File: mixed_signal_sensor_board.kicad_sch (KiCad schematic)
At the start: 51 parts, among them J1 Conn_01x02, J3 Conn_01x04, J4 Conn_01x06, SW1 SW_Push, SW2 SW_Push, U1 LM27762, U2 MagI3C_171013201, U3 TMP117xxDRV, U4 TPS7A20xxxDBV, U5 TPS7A20xxxDBV, U6 ADS131M08xPBS, U7 STM32L552CEUx, Y1 SG-8018CE_8.192M-TJHSA

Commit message: 24V Regulator, Pyro Igniter Circuit
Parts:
- U3: renamed from U2; footprint (none) -> MagI3C_171013201:MagI3C_171013201
- renumbered J3 to J2, J4 to J3, R13 to R12, R12 to R13, R4 to R2, R5 to R3, R2 to R4, R3 to R5, U3 to U1, U1 to U2
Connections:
- no-connect marks 3 -> 20

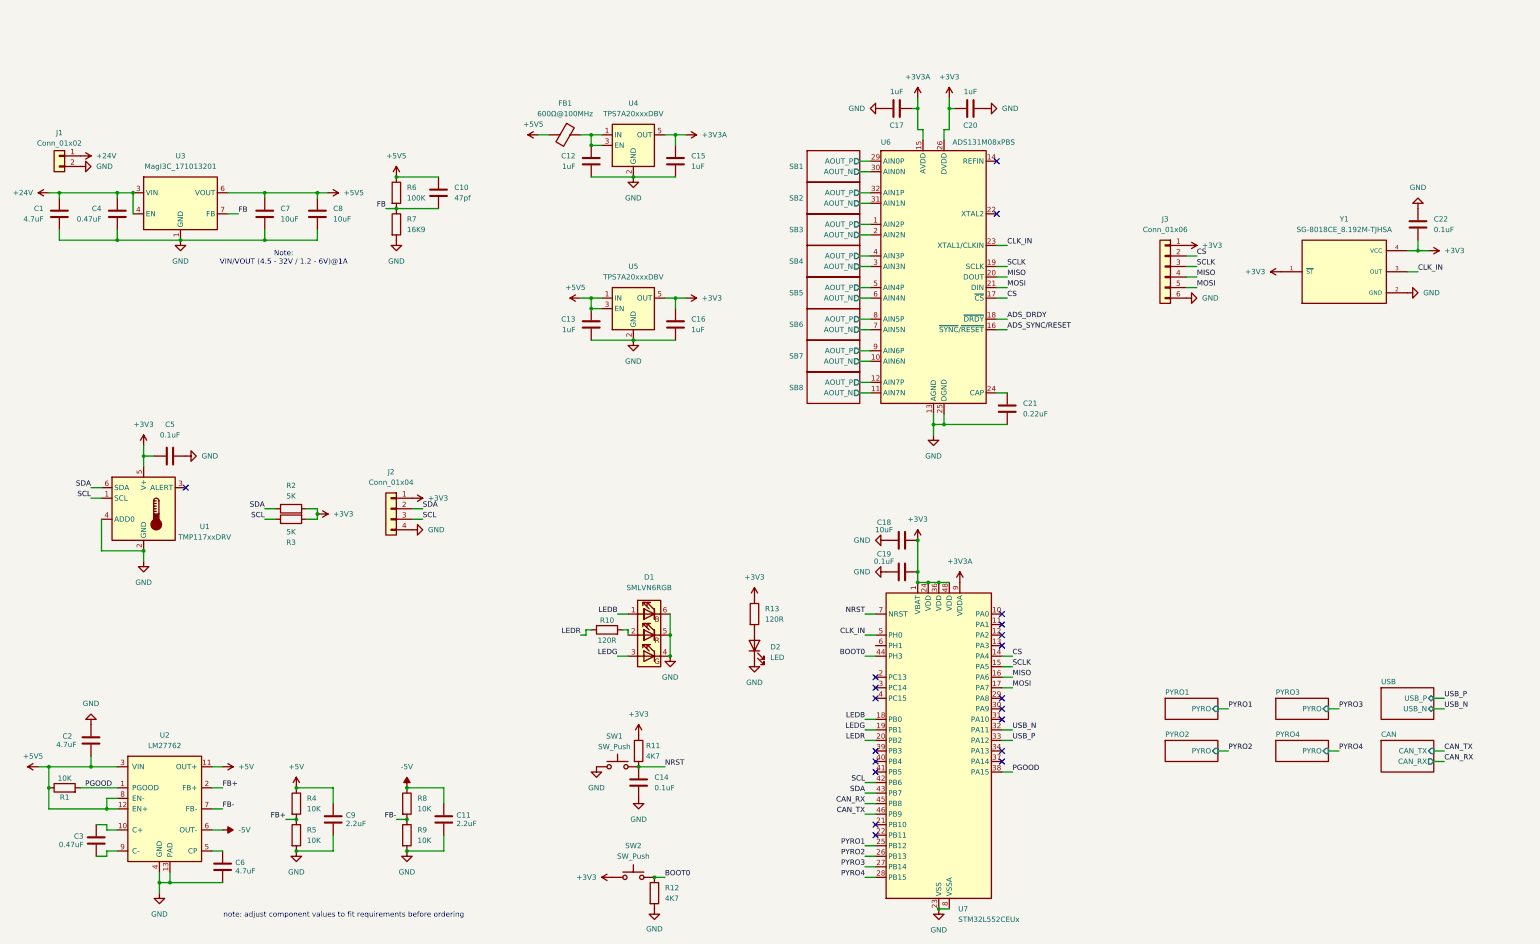
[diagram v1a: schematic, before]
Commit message: Pyro fault detection, Decoupling Caps STM32, Initial PCB Layout
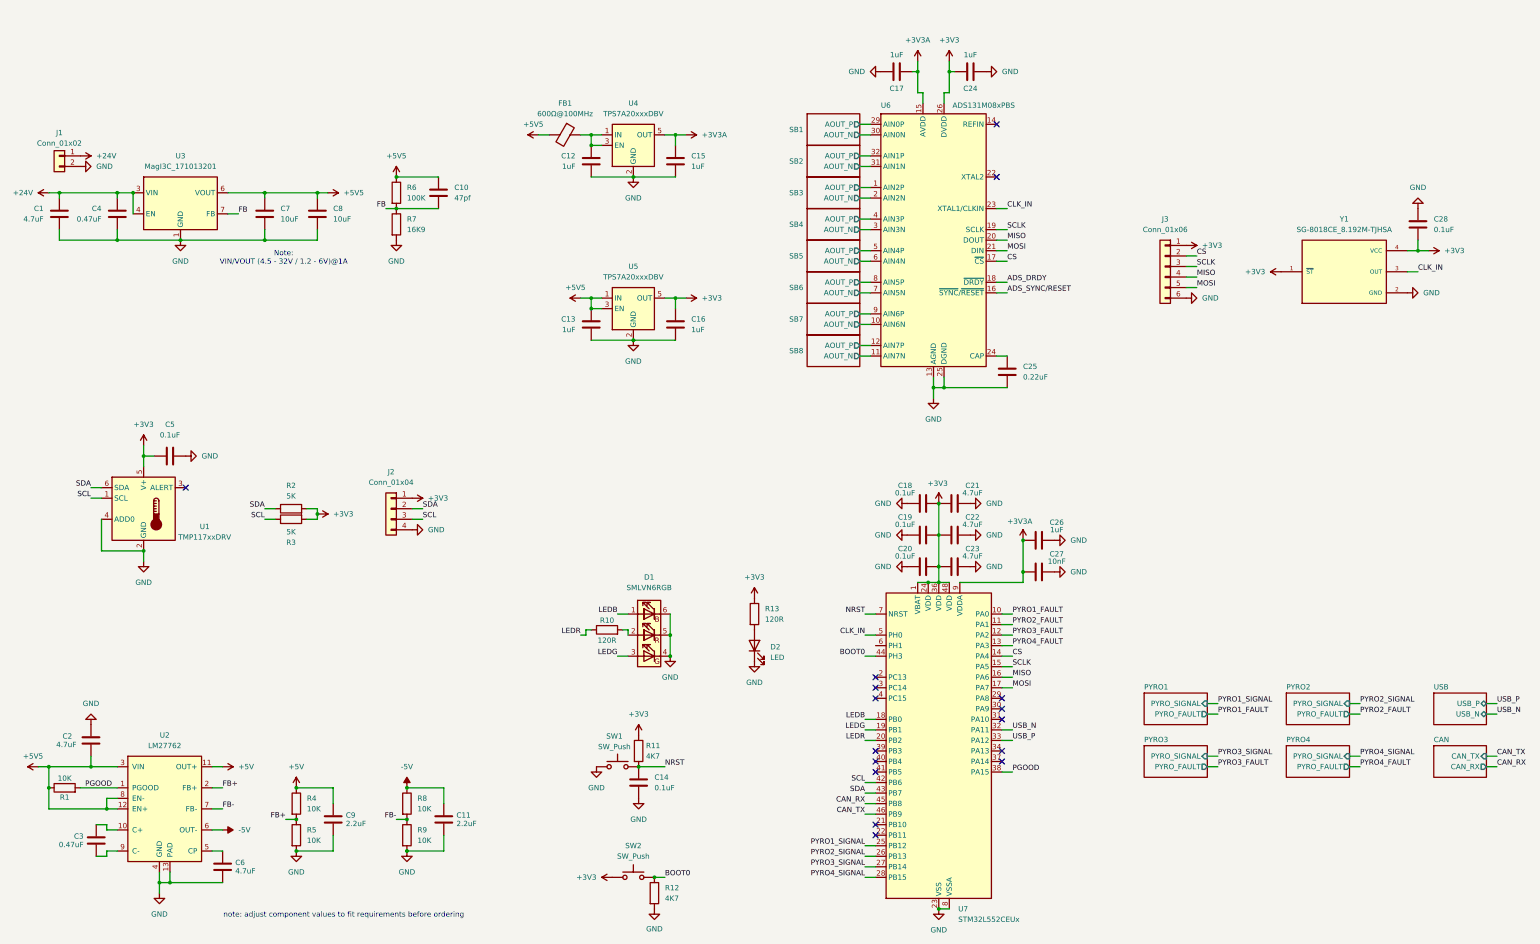
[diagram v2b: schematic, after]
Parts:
- added C20: 0.1uF, Capacitor_SMD:C_0402_1005Metric, symbol Device:C
- added C21, C22, C23: 4.7uF, Capacitor_SMD:C_0402_1005Metric, symbol Device:C
- added C26: 1uF, Capacitor_SMD:C_0402_1005Metric, symbol Device:C
- added C27: 10nF, Capacitor_SMD:C_0402_1005Metric, symbol Device:C
- C18: value 10uF -> 0.1uF
- J1: footprint Connector_JST:JST_XH_B2B-XH-A_1x02_P2.50mm_Vertical -> Connector_JST:JST_XH_S2B-XH-A_1x02_P2.50mm_Horizontal
- J2: footprint Connector_JST:JST_XH_B4B-XH-A_1x04_P2.50mm_Vertical -> Connector_JST:JST_XH_S4B-XH-A_1x04_P2.50mm_Horizontal
- J3: footprint Connector_JST:JST_XH_B6B-XH-A_1x06_P2.50mm_Vertical -> Connector_JST:JST_XH_S6B-XH-A_1x06_P2.50mm_Horizontal
- renumbered C20 to C24, C21 to C25, C22 to C28
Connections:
- net +3V3: now also C20.2, C21.2, C22.2, C23.2
- net +3V3A: now also C26.2, C27.2
- net GND: now also C20.1, C21.1, C22.1, C23.1, C26.1, C27.1
- net PYRO1_FAULT: now reaches U7.10 (PA0)
- net PYRO2_FAULT: now reaches U7.11 (PA1)
- net PYRO3_FAULT: now reaches U7.12 (PA2)
- net PYRO4_FAULT: now reaches U7.13 (PA3)
- net PYRO1 renamed PYRO1_SIGNAL
- net PYRO2 renamed PYRO2_SIGNAL
- net PYRO3 renamed PYRO3_SIGNAL
- net PYRO4 renamed PYRO4_SIGNAL
- no-connect marks 20 -> 16
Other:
- sheet PYRO1 ports: added PYRO_FAULT, PYRO_SIGNAL; removed PYRO
- sheet PYRO2 ports: added PYRO_FAULT, PYRO_SIGNAL; removed PYRO
- sheet PYRO3 ports: added PYRO_FAULT, PYRO_SIGNAL; removed PYRO
- sheet PYRO4 ports: added PYRO_FAULT, PYRO_SIGNAL; removed PYRO
- moved on the sheet: C17, C24, C25, U6

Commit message: Finished first rough initial layout
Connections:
- net ADS_DRDY: now also U7.10 (PA0)
- net ADS_SYNC/RESET: now also U7.11 (PA1)
- net LEDB: now also U7.41 (PB5); no longer U7.18 (PB0)
- net LEDG: now also U7.39 (PB3); no longer U7.19 (PB1)
- net LEDR: now also U7.40 (PB4); no longer U7.20 (PB2)
- net PYRO1_FAULT: now also U7.19 (PB1); no longer U7.10 (PA0)
- net PYRO1_SIGNAL: now also U7.18 (PB0); no longer U7.25 (PB12)
- net PYRO2_FAULT: now also U7.21 (PB10); no longer U7.11 (PA1)
- net PYRO2_SIGNAL: now also U7.20 (PB2); no longer U7.26 (PB13)
- net PYRO3_FAULT: now also U7.28 (PB15); no longer U7.12 (PA2)
- net PYRO3_SIGNAL: now also U7.29 (PA8); no longer U7.27 (PB14)
- net PYRO4_FAULT: now also U7.30 (PA9); no longer U7.13 (PA3)
- net PYRO4_SIGNAL: now also U7.31 (PA10); no longer U7.28 (PB15)
- no-connect marks 16 -> 14

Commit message: Step files, SMD connectors, reduced size
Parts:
- J1: footprint Connector_JST:JST_XH_S2B-XH-A_1x02_P2.50mm_Horizontal -> Connector_JST:JST_PH_S2B-PH-SM4-TB_1x02-1MP_P2.00mm_Horizontal
- J2: footprint Connector_JST:JST_XH_S4B-XH-A_1x04_P2.50mm_Horizontal -> Connector_JST:JST_PH_S4B-PH-SM4-TB_1x04-1MP_P2.00mm_Horizontal
- J3: footprint Connector_JST:JST_XH_S6B-XH-A_1x06_P2.50mm_Horizontal -> Connector_JST:JST_PH_S6B-PH-SM4-TB_1x06-1MP_P2.00mm_Horizontal
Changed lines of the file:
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@@
 			)
 		)
-		(property "Footprint" "Connector_JST:JST_XH_S6B-XH-A_1x06_P2.50mm_Horizontal"
+		(property "Footprint" "Connector_JST:JST_PH_S6B-PH-SM4-TB_1x06-1MP_P2.00mm_Horizontal"
 			(at 309.88 93.98 0)
 			(hide yes)
@@
 			)
 		)
-		(property "Footprint" "Connector_JST:JST_XH_S4B-XH-A_1x04_P2.50mm_Horizontal"
+		(property "Footprint" "Connector_JST:JST_PH_S4B-PH-SM4-TB_1x04-1MP_P2.00mm_Horizontal"
 			(at 123.19 152.4 0)
 			(hide yes)
@@
 			)
 		)
-		(property "Footprint" "Connector_JST:JST_XH_S2B-XH-A_1x02_P2.50mm_Horizontal"
+		(property "Footprint" "Connector_JST:JST_PH_S2B-PH-SM4-TB_1x02-1MP_P2.00mm_Horizontal"
 			(at 43.18 67.31 0)
 			(hide yes)

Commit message: Delvin protection, USB ESD protection, 02x06 pin socket
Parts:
- added D3: D_Zener, Diode_SMD:D_0402_1005Metric, symbol Device:D_Zener
- added J18: Conn_02x06_Odd_Even, Connector_PinSocket_2.54mm:PinSocket_2x06_P2.54mm_Vertical_SMD, symbol Connector_Generic:Conn_02x06_Odd_Even
- added Q5: Q_PMOS, Package_TO_SOT_SMD:SOT-23, symbol Device:Q_PMOS
- added R63: 100K, Resistor_SMD:R_0402_1005Metric, symbol Device:R
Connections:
- net +24V: now also Q5.S; no longer J1.1 (Pin_1)
- net +3V3: now also J18.1 (Pin_1), J18.2 (Pin_2)
- net GND: now also J18.11 (Pin_11), J18.12 (Pin_12), R63.2
- net PA2: now reaches U7.12 (PA2)
- net PA2: now also J18.10 (Pin_10)
- net PA3: now reaches U7.13 (PA3)
- net PA3: now also J18.9 (Pin_9)
- net PC13: now reaches U7.2 (PC13)
- net PC13: now also J18.4 (Pin_4)
- net PB12: now reaches U7.25 (PB12)
- net PB12: now also J18.3 (Pin_3)
- net PB13: now reaches U7.26 (PB13)
- net PB13: now also J18.5 (Pin_5)
- net PB14: now reaches U7.27 (PB14)
- net PB14: now also J18.7 (Pin_7)
- net PC14: now reaches U7.3 (PC14)
- net PC14: now also J18.6 (Pin_6)
- net PC15: now reaches U7.4 (PC15)
- net PC15: now also J18.8 (Pin_8)
- new net: D3.1 (K), J1.1 (Pin_1), Q5.D
- new net: D3.2 (A), Q5.G, R63.1
- no-connect marks 14 -> 6
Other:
- moved on the sheet: J1

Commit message: replaced signal blocks, shortening board, adding precise positioning
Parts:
- removed Q5: Q_PMOS, Package_TO_SOT_SMD:SOT-23, symbol Device:Q_PMOS
- added Q1: IRLML5103TRPBF, Package_TO_SOT_SMD:SOT-23, symbol Transistor_FET:Q_PMOS_GSD
- C1, C4, C7, C8: footprint Capacitor_SMD:C_0402_1005Metric -> Capacitor_SMD:C_0603_1608Metric
- D1: renamed from D3; value D_Zener -> 30V
- renumbered D1 to D2, D2 to D3, J18 to J4, R9 to R10, R10 to R11, R11 to R12, R12 to R13, R13 to R14, R63 to R2, R2 to R3, R3 to R4, R4 to R5, R5 to R6, R6 to R7, R7 to R8, R8 to R9
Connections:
- net +24V: now also Q1.2 (S)
- net SB1/AOUT_N: now also U6.2 (AIN2N); no longer U6.30 (AIN0N)
- net SB1/AOUT_P: now also U6.1 (AIN2P); no longer U6.29 (AIN0P)
- net SB2/AOUT_N: now also U6.3 (AIN3N); no longer U6.31 (AIN1N)
- net SB2/AOUT_P: now also U6.4 (AIN3P); no longer U6.32 (AIN1P)
- net SB3/AOUT_N: now also U6.6 (AIN4N); no longer U6.2 (AIN2N)
- net SB3/AOUT_P: now also U6.5 (AIN4P); no longer U6.1 (AIN2P)
- net SB4/AOUT_N: now also U6.7 (AIN5N); no longer U6.3 (AIN3N)
- net SB4/AOUT_P: now also U6.8 (AIN5P); no longer U6.4 (AIN3P)
- net SB5/AOUT_N: now also U6.11 (AIN7N); no longer U6.6 (AIN4N)
- net SB5/AOUT_P: now also U6.12 (AIN7P); no longer U6.5 (AIN4P)
- net SB6/AOUT_N: now also U6.10 (AIN6N); no longer U6.7 (AIN5N)
- net SB6/AOUT_P: now also U6.9 (AIN6P); no longer U6.8 (AIN5P)
- net SB7/AOUT_N: now also U6.31 (AIN1N); no longer U6.10 (AIN6N)
- net SB7/AOUT_P: now also U6.32 (AIN1P); no longer U6.9 (AIN6P)
- net SB8/AOUT_N: now also U6.30 (AIN0N); no longer U6.11 (AIN7N)
- net SB8/AOUT_P: now also U6.29 (AIN0P); no longer U6.12 (AIN7P)
- net at D1.1 (K), J1.1 (Pin_1): now also Q1.3 (D)
- net at D1.2 (A), R2.1: now also Q1.1 (G)

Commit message: Compact board, Artistic Freedom
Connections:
- net +3V3: now also J3.6 (Pin_6); no longer J3.1 (Pin_1)
- net CS: now also J3.5 (Pin_5); no longer J3.2 (Pin_2)
- net GND: now also J3.1 (Pin_1); no longer J3.6 (Pin_6)
- net MISO: now also J3.3 (Pin_3); no longer J3.4 (Pin_4)
- net MOSI: now also J3.2 (Pin_2); no longer J3.5 (Pin_5)
- net SCLK: now also J3.4 (Pin_4); no longer J3.3 (Pin_3)

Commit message: removed SPI, I2C, compacting pyro channels, new pyro schematic
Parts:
- removed J2: Conn_01x04, Connector_JST:JST_PH_S4B-PH-SM4-TB_1x04-1MP_P2.00mm_Horizontal, symbol Connector_Generic:Conn_01x04
- removed J4: Conn_02x06_Odd_Even, Connector_PinSocket_2.54mm:PinSocket_2x06_P2.54mm_Vertical_SMD, symbol Connector_Generic:Conn_02x06_Odd_Even
- D1: value 30V -> 24V
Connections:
- net PC13 is gone; now on net ADS_DRDY: U7.2 (PC13)
- net PC14 is gone; now on net ADS_SYNC/RESET: U7.3 (PC14)
- net +24V: now also D1.1 (K)
- net ADS_DRDY: no longer U7.10 (PA0)
- net ADS_SYNC/RESET: no longer U7.11 (PA1)
- net CLK_IN: no longer U7.5 (PH0)
- net at J1.1 (Pin_1), Q1.3 (D): no longer D1.1 (K)
- net PA2: no longer names the net of U7.12 (PA2)
- net PA3: no longer names the net of U7.13 (PA3)
- net PB12: no longer names the net of U7.25 (PB12)
- net PB13: no longer names the net of U7.26 (PB13)
- net PB14: no longer names the net of U7.27 (PB14)
- net PC15: no longer names the net of U7.4 (PC15)
- no-connect marks 6 -> 15
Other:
- moved on the sheet: D1, Q1, R2
